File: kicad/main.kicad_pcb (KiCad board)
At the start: 2 copper layers, 15 parts, among them J1 Barrel_Jack, J2 Conn, J3 VIA1, J4 VIA2, U1 DS1813-5+, U2 W65C816SxP, U3 L7805, U4 ATF16V8, U5 AS6C4008-55PCN, U6 27C512, U7 74LS573, U8 W65C22NxP, U9 74HC245, X1 CXO_DIP14

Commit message: v0.1 PCB
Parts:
- added C1: 0.1uF, Capacitor_THT:C_Disc_D3.0mm_W1.6mm_P2.50mm, F.Cu at (36.8, 22.9)
- added C2: 0.1uF, my:C_Disc_VeryLong, F.Cu at (58.4, 49.5)
- added C3: 0.1uF, my:C_Disc_VeryLong, F.Cu at (81.3, 35.6)
- added C4: 0.1uF, my:C_Disc_VeryLong, F.Cu at (104.1, 40.6)
- added C5: 0.1uF, my:C_Disc_Long, F.Cu at (33.0, 90.2)
- added C6: 0.1uF, my:C_Disc_Long, F.Cu at (33.0, 105.4)
- added C7: 0.1uF, my:C_Disc_Long, F.Cu at (63.5, 105.4)
- added C8: 10uF, Capacitor_THT:CP_Radial_D6.3mm_P2.50mm, F.Cu at (100.3, 102.9)
- added U10: 74HC14, Package_DIP:DIP-14_W7.62mm_Socket, F.Cu at (58.4, 94.0)
- U6: footprint Package_DIP:DIP-28_W15.24mm_Socket -> my:ZIF28
- U7: value 74LS573 -> 74HC573
- moved J2 113.3 mm to (27.9, 115.6), turned to 90 degrees
- moved U4 91.8 mm to (27.9, 109.2), turned to 90 degrees
- moved U9 88.7 mm to (58.4, 109.2), turned to 90 degrees
- moved U7 85.9 mm to (27.9, 94.0), turned to 90 degrees
- moved U8 74.5 mm to (111.8, 73.7), turned to 180 degrees
- moved U3 72.5 mm to (109.2, 102.9)
- moved U6 65.7 mm to (27.9, 38.1)
- moved J1 57.8 mm to (106.0, 114.3), turned to 90 degrees
- moved U2 55.9 mm to (66.0, 73.7), turned to 180 degrees
- moved U1 50.4 mm to (80.0, 74.9)
- moved X1 49.5 mm to (83.8, 94.0)
- moved RN1 42.3 mm to (50.8, 81.3)
- moved J3 33.5 mm to (116.8, 88.9), turned to 180 degrees
- moved U5 30.3 mm to (73.7, 25.4)
- moved J4 2.84 mm to (116.8, 53.3), turned to 180 degrees
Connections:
- U2 pad 39: unconnected-(U2-VDA-Pad39) -> VDA
- U4 pad 13: ~{CLK} -> Net-(U4-IO7)
- U4 pad 14: CLK -> Net-(U4-IO6)
- U8 pad 24: +5V -> VDA
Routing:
- net GND: track 0.00 -> 128.2 mm
- net +5V: track 0.00 -> 87.1 mm
- net Net-(U3-IN): track 0.00 -> 12.8 mm
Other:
- board outline added: 100 x 100 mm
- board text added: "65c816 SBC"
- board text added: "Farland"
- board text added: "by Andrew Dunai v1.0"

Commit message: v0.1 final PCB
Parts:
- removed J2: Conn, Connector_PinHeader_2.54mm:PinHeader_1x05_P2.54mm_Vertical
- removed J4: VIA2, Connector_PinHeader_2.54mm:PinHeader_1x12_P2.54mm_Vertical
- removed the U7 at (27.9, 94.0)
- added H1: MountingHole_Pad, MountingHole:MountingHole_2.5mm_Pad, F.Cu at (18.1, -13.3)
- added H2: MountingHole_Pad, MountingHole:MountingHole_2.5mm_Pad, F.Cu at (112.1, -13.3)
- added LCD1: ~, my:2004A-OLED, F.Cu at (16.6, -109.8)
- added U6: 74HC273, Package_DIP:DIP-20_W7.62mm_Socket, F.Cu at (48.6, -102.2)
- moved C5 188.3 mm to (52.4, -97.1), turned to -90 degrees
- moved C7 162.3 mm to (52.4, -56.5), turned to 90 degrees
- moved U7 160.7 mm to (56.2, -51.4), turned to 180 degrees
- moved C6 157.7 mm to (84.1, -43.8)
- moved U5 157.7 mm to (79.1, -40.0)
- moved J3 155.6 mm to (112.1, -66.7)
- moved RN1 143.8 mm to (19.4, -59.0), turned to 90 degrees
- moved J1 137.9 mm to (101.2, -23.5)
- moved C8 137.8 mm to (99.4, -34.9)
- moved U8 135.3 mm to (107.0, -32.4)
- moved U9 130.5 mm to (70.2, -55.2)
- moved C2 130.1 mm to (33.3, -78.1)
- moved U1 130.1 mm to (41.0, -54.0)
- moved C3 128.0 mm to (71.4, -92.1)
- moved C4 128.0 mm to (94.3, -87.0)
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- renumbered U2 to U1, U5 to U2, U6 to U3, U8 to U4, U4 to U5, U9 to U7, U3 to U8, U1 to U9
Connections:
- U10 pad 1: Net-(U4-IO6) -> Net-(U5-IO7)
- U10 pad 3: Net-(U4-IO7) -> Net-(U5-IO8)
- U4 pad 10: Net-(J4-Pin_3) -> unconnected-(U4-PB0-Pad10)
- U4 pad 11: Net-(J4-Pin_4) -> unconnected-(U4-PB1-Pad11)
- U4 pad 12: Net-(J4-Pin_5) -> unconnected-(U4-PB2-Pad12)
- U4 pad 13: Net-(J4-Pin_6) -> unconnected-(U4-PB3-Pad13)
- U4 pad 14: Net-(J4-Pin_7) -> unconnected-(U4-PB4-Pad14)
- U4 pad 15: Net-(J4-Pin_8) -> unconnected-(U4-PB5-Pad15)
- U4 pad 16: Net-(J4-Pin_9) -> unconnected-(U4-PB6-Pad16)
- U4 pad 17: Net-(J4-Pin_10) -> unconnected-(U4-PB7-Pad17)
- U4 pad 18: Net-(J4-Pin_11) -> unconnected-(U4-CB1-Pad18)
- U4 pad 19: Net-(J4-Pin_12) -> unconnected-(U4-CB2-Pad19)
- U5 pad 12: unconnected-(U4-IO8-Pad12) -> Net-(U5-IO8)
- U5 pad 13: Net-(U4-IO7) -> Net-(U5-IO7)
- U5 pad 14: Net-(U4-IO6) -> ~{WD}
- U5 pad 15: ~{WD} -> ~{RD}
- U5 pad 16: ~{RD} -> LCDEN
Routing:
- net GND: track 128.2 -> 119.1 mm
- net +5V: track 87.1 -> 80.7 mm
- net Net-(U8-IN): track 12.8 -> 12.2 mm

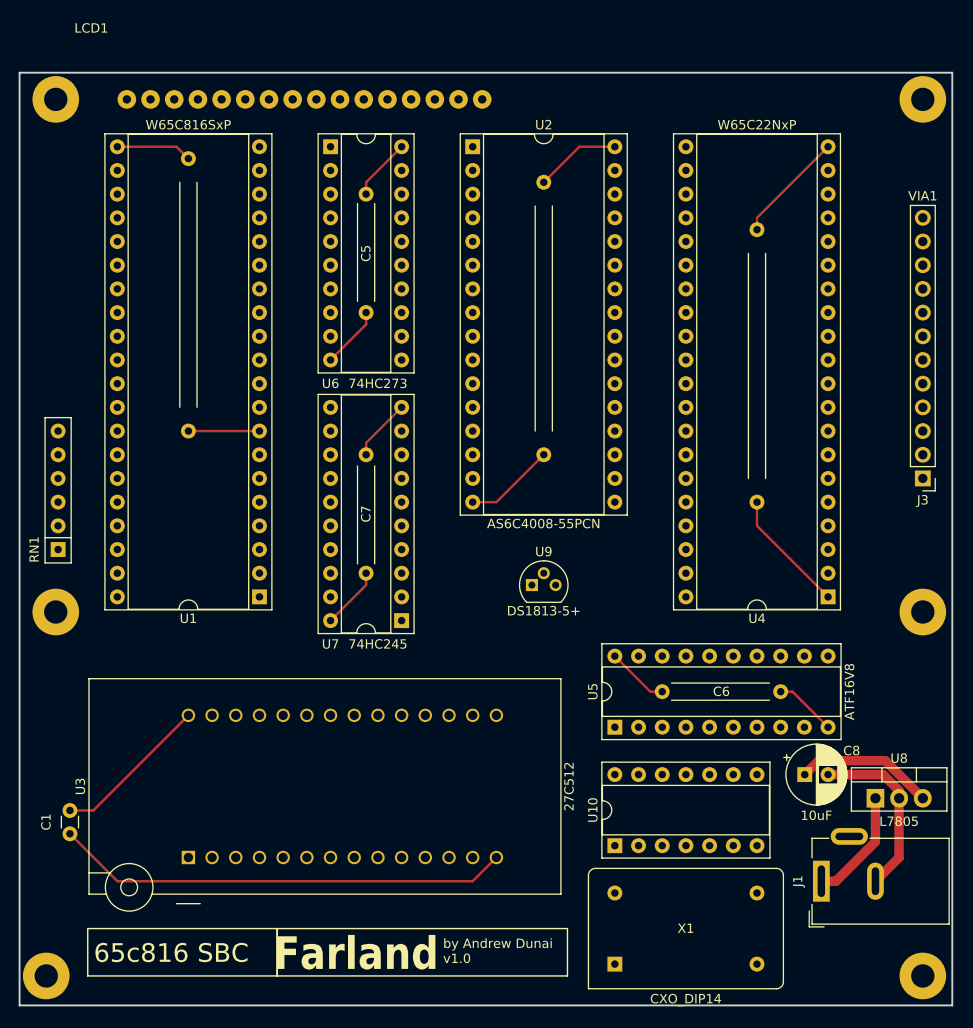
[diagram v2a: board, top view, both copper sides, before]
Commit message: Add 74HC00 for R/W qualification to save ATF pins for slow mode
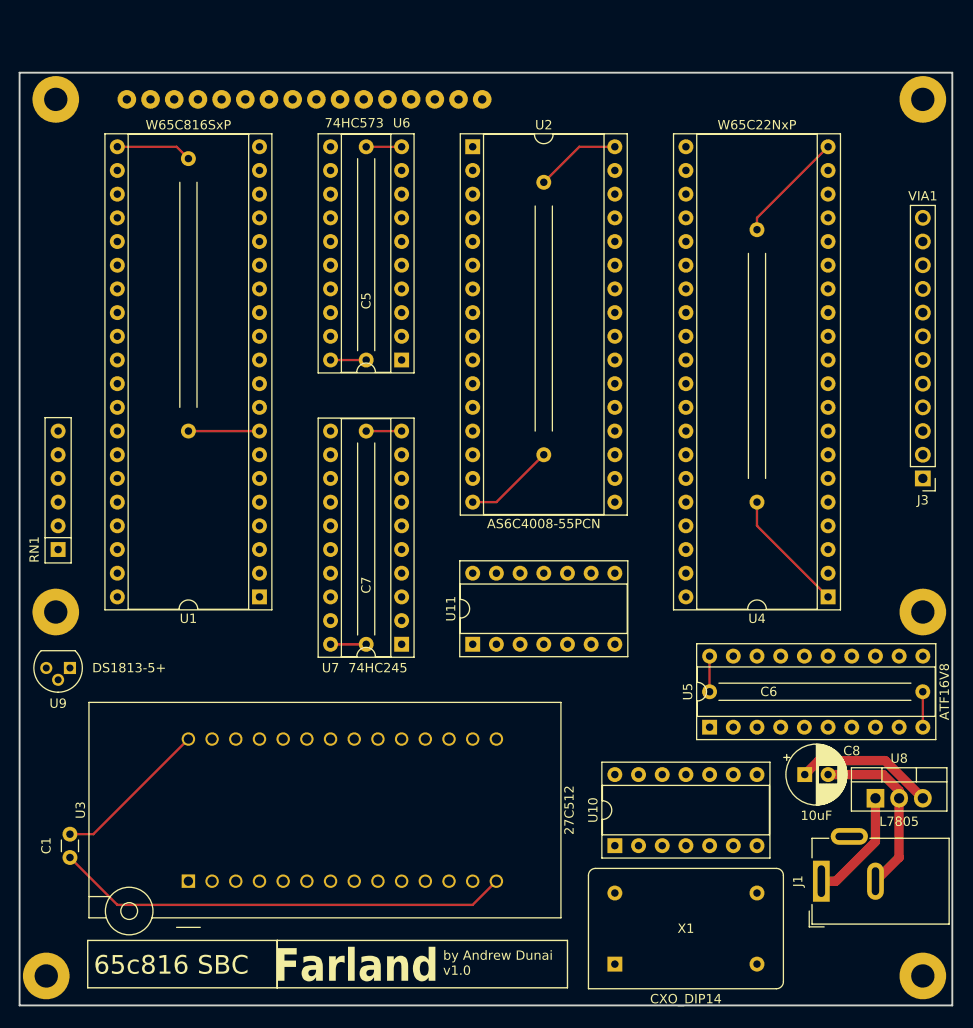
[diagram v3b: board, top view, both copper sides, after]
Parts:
- added U11: 74HC00, Package_DIP:DIP-14_W7.62mm_Socket, F.Cu at (63.8, -48.9)
- U6: value 74HC273 -> 74HC573
- moved U9 50.3 mm to (20.6, -46.3), turned to 180 degrees
- moved U6 24.1 mm to (56.2, -79.4), turned to 180 degrees
- moved C5 17.8 mm to (52.4, -79.4), turned to 90 degrees
- moved U5 10.2 mm to (89.2, -40.0)
- moved C7 7.63 mm to (52.4, -48.9)
- moved C6 5.08 mm to (89.2, -43.8)
- moved C1 2.54 mm to (20.6, -28.5)
- moved U3 2.54 mm to (33.3, -23.5)
- moved U7 2.54 mm to (56.2, -48.9)
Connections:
- U5 pad 14: ~{WD} -> unconnected-(U5-IO6-Pad14)
- U5 pad 15: ~{RD} -> unconnected-(U5-IO5-Pad15)
- U5 pad 9: R~{W} -> unconnected-(U5-I9-Pad9)
- U6 pad 1: ~{RES} -> GND
- U6 pad 11: CLK -> ~{CLK}
- U6 pad 12: A_{20} -> A_{23}
- U6 pad 13: DB_{4} -> A_{22}
- U6 pad 14: DB_{5} -> A_{21}
- U6 pad 15: A_{21} -> A_{20}
- U6 pad 16: A_{22} -> A_{19}
- U6 pad 17: DB_{6} -> A_{18}
- U6 pad 18: DB_{7} -> A_{17}
- U6 pad 19: A_{23} -> A_{16}
- U6 pad 2: A_{16} -> DB_{0}
- U6 pad 3: DB_{0} -> DB_{1}
- U6 pad 4: DB_{1} -> DB_{2}
- U6 pad 5: A_{17} -> DB_{3}
- U6 pad 6: A_{18} -> DB_{4}
- U6 pad 7: DB_{2} -> DB_{5}
- U6 pad 8: DB_{3} -> DB_{6}
- U6 pad 9: A_{19} -> DB_{7}
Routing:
- net GND: track 119.1 -> 110.6 mm
- net +5V: track 80.7 -> 72.2 mm
